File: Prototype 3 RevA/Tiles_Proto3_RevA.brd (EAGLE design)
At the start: 40 x 40 mm, 40 parts, among them U2 MF-DSC-SOT233-MMBT3904

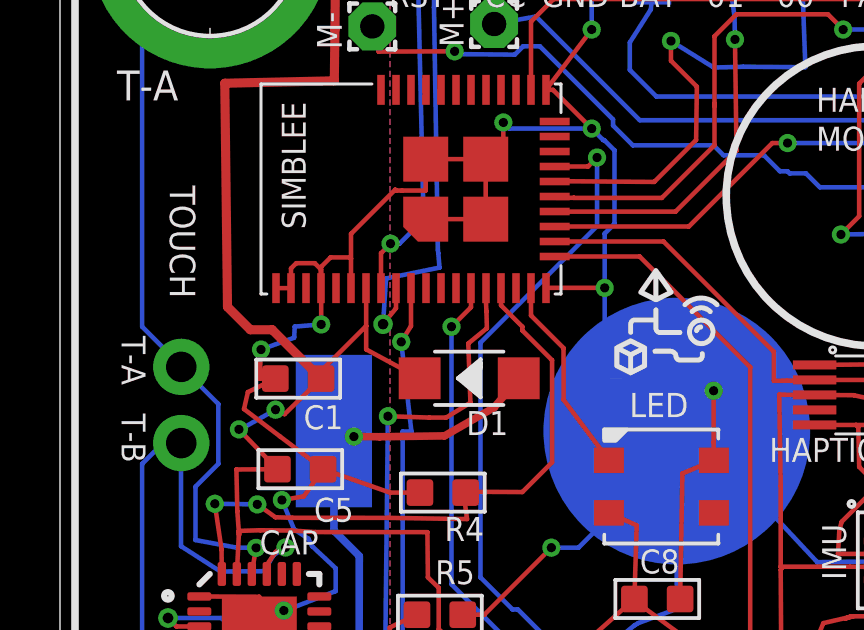
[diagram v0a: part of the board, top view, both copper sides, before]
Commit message: switched imu from LSM9DS1 to ADXL345
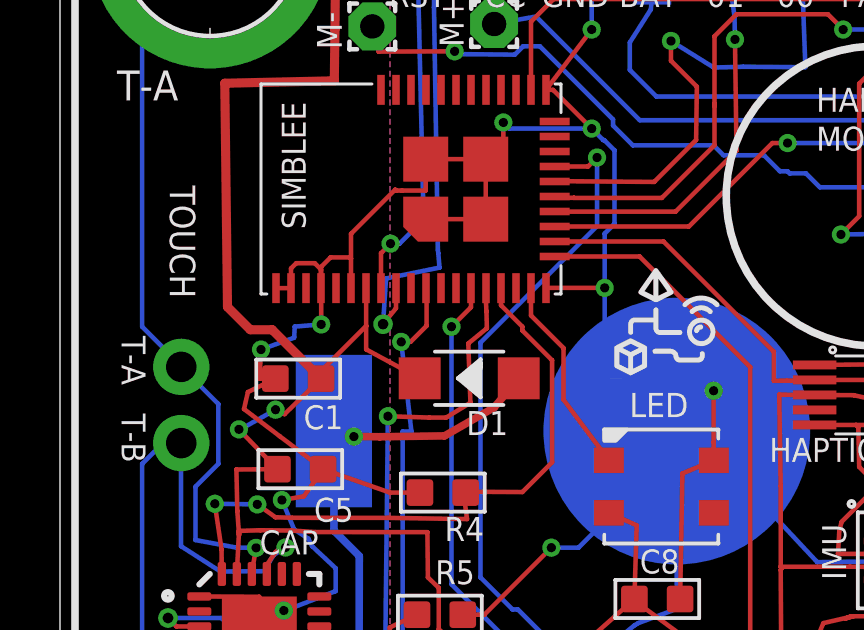
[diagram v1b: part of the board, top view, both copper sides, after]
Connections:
- removed net PWRBTN: SIMBLEE.12
- net STATLED: now also SIMBLEE.11; no longer SIMBLEE.10
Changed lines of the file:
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@@
 <setting verticaltext="up"/>
 </settings>
-<grid distance="1" unitdist="mm" unit="mm" style="lines" multiple="1" display="yes" altdistance="0.01" altunitdist="mm" altunit="mm"/>
+<grid distance="10" unitdist="mil" unit="mil" style="lines" multiple="1" display="yes" altdistance="0.01" altunitdist="mm" altunit="mm"/>
 <layers>
 <layer number="1" name="Top" color="4" fill="1" visible="yes" active="yes"/>
@@
 <layer number="14" name="Route14" color="1" fill="6" visible="no" active="no"/>
 <layer number="15" name="Route15" color="4" fill="6" visible="no" active="no"/>
-<layer number="16" name="Bottom" color="1" fill="1" visible="no" active="yes"/>
+<layer number="16" name="Bottom" color="1" fill="1" visible="yes" active="yes"/>
 <layer number="17" name="Pads" color="2" fill="1" visible="yes" active="yes"/>
 <layer number="18" name="Vias" color="2" fill="1" visible="yes" active="yes"/>
@@
 <layer number="20" name="Dimension" color="15" fill="1" visible="yes" active="yes"/>
 <layer number="21" name="tPlace" color="7" fill="1" visible="yes" active="yes"/>
-<layer number="22" name="bPlace" color="7" fill="1" visible="no" active="yes"/>
+<layer number="22" name="bPlace" color="7" fill="1" visible="yes" active="yes"/>
 <layer number="23" name="tOrigins" color="15" fill="1" visible="yes" active="yes"/>
-<layer number="24" name="bOrigins" color="15" fill="1" visible="no" active="yes"/>
+<layer number="24" name="bOrigins" color="15" fill="1" visible="yes" active="yes"/>
 <layer number="25" name="tNames" color="7" fill="1" visible="yes" active="yes"/>
-<layer number="26" name="bNames" color="7" fill="1" visible="no" active="yes"/>
+<layer number="26" name="bNames" color="7" fill="1" visible="yes" active="yes"/>
 <layer number="27" name="tValues" color="7" fill="1" visible="yes" active="yes"/>
-<layer number="28" name="bValues" color="7" fill="1" visible="no" active="yes"/>
+<layer number="28" name="bValues" color="7" fill="1" visible="yes" active="yes"/>
 <layer number="29" name="tStop" color="7" fill="3" visible="no" active="yes"/>
 <layer number="30" name="bStop" color="7" fill="6" visible="no" active="yes"/>
@@
 <layer number="38" name="bTest" color="7" fill="1" visible="no" active="yes"/>
 <layer number="39" name="tKeepout" color="4" fill="11" visible="yes" active="yes"/>
-<layer number="40" name="bKeepout" color="1" fill="11" visible="no" active="yes"/>
+<layer number="40" name="bKeepout" color="1" fill="11" visible="yes" active="yes"/>
 <layer number="41" name="tRestrict" color="4" fill="10" visible="yes" active="yes"/>
-<layer number="42" name="bRestrict" color="1" fill="10" visible="no" active="yes"/>
+<layer number="42" name="bRestrict" color="1" fill="10" visible="yes" active="yes"/>
 <layer number="43" name="vRestrict" color="2" fill="10" visible="no" active="yes"/>
 <layer number="44" name="Drills" color="7" fill="1" visible="yes" active="yes"/>
@@
 <layer number="50" name="dxf" color="7" fill="1" visible="no" active="no"/>
 <layer number="51" name="tDocu" color="7" fill="1" visible="yes" active="yes"/>
-<layer number="52" name="bDocu" color="7" fill="1" visible="no" active="yes"/>
+<layer number="52" name="bDocu" color="7" fill="1" visible="yes" active="yes"/>
 <layer number="53" name="tGND_GNDA" color="7" fill="9" visible="no" active="no"/>
 <layer number="54" name="bGND_GNDA" color="1" fill="9" visible="no" active="no"/>
@@
 <element name="C1" library="Seeed-OPL-Capacitor" package="C0603" value="1uf" x="7.94" y="-19.34" smashed="yes" rot="R270">
 <attribute name="MPN" value="CC0603KRX5R6BB106" x="7.94" y="-19.34" size="1.778" layer="27" rot="R270" display="off"/>
-<attribute name="NAME" x="9.4386" y="-20.229" size="0.8" layer="25" ratio="11" rot="R180"/>
 <attribute name="NAME" x="9.21" y="-19.086" size="0.635" layer="33" ratio="10" rot="R180"/>
+<attribute name="NAME" x="9.4386" y="-20.229" size="0.8" layer="25" ratio="11" rot="R180"/>
 <attribute name="VALUE" x="9.21" y="-17.7525" size="0.635" layer="27" ratio="10" rot="R180"/>
 </element>
 <element name="C2" library="Seeed-OPL-Capacitor" package="C0603" value="100nf" x="33.03" y="-26.37" smashed="yes" rot="R90">
 <attribute name="MPN" value="CC0603KRX7R9BB104" x="33.03" y="-26.37" size="1.778" layer="27" rot="R90" display="off"/>
-<attribute name="NAME" x="31.76" y="-25.481" size="0.8" layer="25" ratio="11"/>
 <attribute name="NAME" x="31.76" y="-26.624" size="0.635" layer="33" ratio="10"/>
+<attribute name="NAME" x="31.76" y="-25.481" size="0.8" layer="25" ratio="11"/>
 <attribute name="VALUE" x="31.76" y="-27.9575" size="0.635" layer="27" ratio="10"/>
 </element>
 <element name="C3" library="Seeed-OPL-Capacitor" package="C0603" value="10uf" x="33.04" y="-24.03" smashed="yes" rot="R90">
 <attribute name="MPN" value="CC0603KRX5R6BB106" x="33.04" y="-24.03" size="1.778" layer="27" rot="R90" display="off"/>
-<attribute name="NAME" x="31.77" y="-23.141" size="0.8" layer="25" ratio="11"/>
 <attribute name="NAME" x="31.77" y="-24.284" size="0.635" layer="33" ratio="10"/>
+<attribute name="NAME" x="31.77" y="-23.141" size="0.8" layer="25" ratio="11"/>
 <attribute name="VALUE" x="31.77" y="-25.6175" size="0.635" layer="27" ratio="10"/>
 </element>
 <element name="C4" library="Seeed-OPL-Capacitor" package="C0603" value="220nf" x="32.97" y="-21.52" smashed="yes" rot="R90">
 <attribute name="MPN" value="CC0603KRX7R8BB224" x="32.97" y="-21.52" size="1.778" layer="27" rot="R90" display="off"/>
-<attribute name="NAME" x="31.7" y="-20.631" size="0.8" layer="25" ratio="11"/>
 <attribute name="NAME" x="31.7" y="-21.774" size="0.635" layer="33" ratio="10"/>
+<attribute name="NAME" x="31.7" y="-20.631" size="0.8" layer="25" ratio="11"/>
 <attribute name="VALUE" x="31.7" y="-23.1075" size="0.635" layer="27" ratio="10"/>
 </element>
 <element name="C5" library="Seeed-OPL-Capacitor" package="C0603" value="10uf" x="8.01" y="-22.36" smashed="yes" rot="R90">
 <attribute name="MPN" value="CC0603KRX5R6BB106" x="8.01" y="-22.36" size="1.778" layer="27" rot="R90" display="off"/>
-<attribute name="NAME" x="8.4672" y="-24.1126" size="0.8" layer="25" ratio="11"/>
 <attribute name="NAME" x="6.74" y="-22.614" size="0.635" layer="33" ratio="10"/>
+<attribute name="NAME" x="8.4672" y="-24.1126" size="0.8" layer="25" ratio="11"/>
 <attribute name="VALUE" x="6.74" y="-23.9475" size="0.635" layer="27" ratio="10"/>
 </element>
 <element name="C6" library="Seeed-OPL-Capacitor" package="C0603" value="1uf" x="33.23" y="-12.77" smashed="yes">
 <attribute name="MPN" value="CC0603KRX7R8BB105" x="33.23" y="-12.77" size="1.778" layer="27" display="off"/>
-<attribute name="NAME" x="34.1952" y="-12.3382" size="0.8" layer="25" ratio="11" rot="R270"/>
 <attribute name="NAME" x="32.976" y="-11.5" size="0.635" layer="33" ratio="10" rot="R270"/>
+<attribute name="NAME" x="34.1952" y="-12.3382" size="0.8" layer="25" ratio="11" rot="R270"/>
 <attribute name="VALUE" x="31.6425" y="-11.5" size="0.635" layer="27" ratio="10" rot="R270"/>
 </element>
 <element name="C7" library="Seeed-OPL-Capacitor" package="C0603" value="1uf" x="32.048075" y="-16.88535625" smashed="yes" rot="R315">
 <attribute name="MPN" value="CC0603KRX7R8BB105" x="32.048075" y="-16.88535625" size="1.778" layer="27" rot="R315" display="off"/>
-<attribute name="NAME" x="32.685715625" y="-17.55575" size="0.8" layer="25" ratio="11" rot="R225"/>
 <attribute name="NAME" x="32.76649375" y="-15.807728125" size="0.635" layer="33" ratio="10" rot="R225"/>
+<attribute name="NAME" x="32.685715625" y="-17.55575" size="0.8" layer="25" ratio="11" rot="R225"/>
 <attribute name="VALUE" x="31.823565625" y="-14.8648" size="0.635" layer="27" ratio="10" rot="R225"/>
 </element>
@@
 <element name="C8" library="Seeed-OPL-Capacitor" package="C0603" value="1uf" x="19.9088" y="-26.6864" smashed="yes" rot="R270">
 <attribute name="MPN" value="CC0603KRX7R8BB105" x="19.9088" y="-26.6864" size="1.778" layer="27" rot="R270" display="off"/>
-<attribute name="NAME" x="20.6454" y="-25.0354" size="0.8" layer="25" ratio="11" rot="R180"/>
 <attribute name="NAME" x="21.1788" y="-26.4324" size="0.635" layer="33" ratio="10" rot="R180"/>
+<attribute name="NAME" x="20.6454" y="-25.0354" size="0.8" layer="25" ratio="11" rot="R180"/>
 <attribute name="VALUE" x="21.1788" y="-25.0989" size="0.635" layer="27" ratio="10" rot="R180"/>
 </element>
@@
 <wire x1="16.7842" y1="-20.0442" x2="18.2958" y2="-22.0638" width="0.1524" layer="1"/>
 </signal>
-<signal name="PWRBTN">
-<contactref element="SIMBLEE" pad="12"/>
-</signal>
 <signal name="STATLED">
-<contactref element="SIMBLEE" pad="10"/>
 <contactref element="R6" pad="P$1"/>
-<wire x1="11.7" y1="-16.325" x2="11.7" y2="-17.5888" width="0.1524" layer="1"/>
-<wire x1="11.7" y1="-17.5888" x2="11.374" y2="-18.1148" width="0.1524" layer="1"/>
 <via x="11.374" y="-18.1148" extent="1-16" drill="0.3048"/>
 <wire x1="11.374" y1="-18.1148" x2="11.714" y2="-21.1055375" width="0.1524" layer="16"/>
@@
 <wire x1="12.2122" y1="-30.8434" x2="12.2122" y2="-32.3378" width="0.1524" layer="1"/>
 <wire x1="12.2122" y1="-32.3378" x2="11.75" y2="-32.8" width="0.1524" layer="1"/>
+<contactref element="SIMBLEE" pad="11"/>
+<wire x1="11.374" y1="-18.1148" x2="11.6852" y2="-18.1148" width="0.1524" layer="1"/>
+<wire x1="11.6852" y1="-18.1148" x2="12.22" y2="-17.58" width="0.1524" layer="1"/>
+<wire x1="12.22" y1="-17.58" x2="12.22" y2="-16.345" width="0.1524" layer="1"/>
+<wire x1="12.22" y1="-16.345" x2="12.2" y2="-16.325" width="0.1524" layer="1"/>
 </signal>
 <signal name="BUZZER">

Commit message: p3rA and dock p1rA sent to production
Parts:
- removed C3: 10uf, Seeed-OPL-Capacitor:C0603
- removed C4: 220nf, Seeed-OPL-Capacitor:C0603
- IMU: value LSM9DS1 -> ADXL345BCCZ-RL; device LSM9DS1:LGA24_3.5X3.1MM -> Seeed-OPL-sensor:LGA14-0.8-5.0X3.0MM
- moved C2 2.21 mm to (32.8, -24.2)
- moved IMU 1.38 mm to (27.6, -24.3), turned to 90 degrees
- moved BUZZER 1.27 mm to (34.2, -28.7)
- moved BATT_CHG 0.96 mm to (19.2, -6.97)
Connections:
- removed net N$1: C3.1, IMU.21
- removed net N$10: IMU.10
- removed net N$12: IMU.12
- removed net N$2: C4.1, IMU.24
- net GND: now also IMU.2, IMU.4, IMU.5; no longer C3.2, C4.2, IMU.14, IMU.15, IMU.16, IMU.17, IMU.18, IMU.19, IMU.20
- net IMU-INT: now also IMU.8; no longer IMU.11
- net SCL: now also IMU.14; no longer IMU.2
- net SDA: now also IMU.13; no longer IMU.4
- net VCC: now also IMU.6; no longer IMU.13, IMU.22, IMU.23, IMU.3, IMU.8
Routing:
- net N$2: track 8.23 -> 0.00 mm
- net VCC: track 167.6 -> 160.6 mm, vias 6 -> 4
- net N$1: track 5.33 -> 0.00 mm
- net GND: track 177.3 -> 180.3 mm, vias 20 -> 18
- net SDA: track 77.5 -> 76.5 mm
- net V_BATT: track 108.0 -> 107.2 mm
- net N$6: track 0.84 -> 1.64 mm
- net SCL: track 75.4 -> 76.2 mm
- net IMU-INT: track 27.2 -> 26.5 mm
- net N$4: track 10.0 -> 9.38 mm
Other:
- board text added: "/Users/Simone/Downloads/digi.bmp"
